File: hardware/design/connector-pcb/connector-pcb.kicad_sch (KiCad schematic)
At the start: 7 parts, among them J1 JWPF B04B, J2 JWPF B03B/B02B, J3 Conn_01x03_Pin, J5 Conn_01x02_Pin, J6 Conn_01x02_Pin, J8 JWPF B03B/B02B, J9 Conn_01x03_Pin

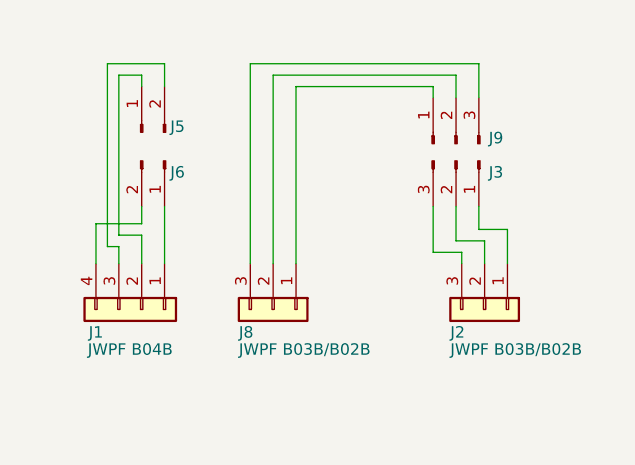
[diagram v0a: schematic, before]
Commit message: Gen2.1 final hardware design (#16)
* New schematic done

Works with TLIN1028-Q1 transceiver
Added BMP581 pressure sensor
Removed 3wire output stage

* FInal ordered hardware

New 3pin connector
Extra 2pin connector for cadence measurement
No 3pin sensor variant
DC/DC converter for MCU
Pressure sensor
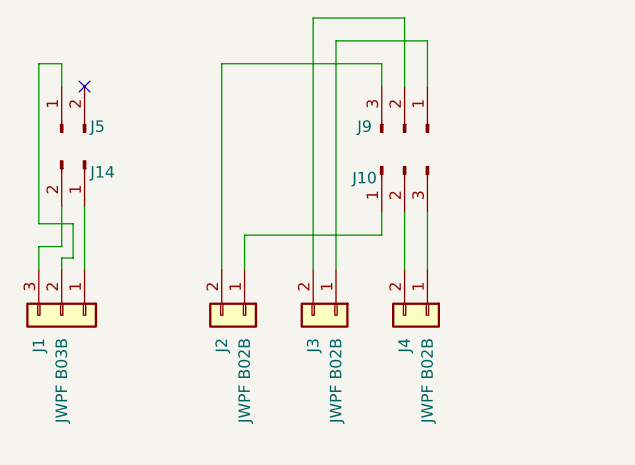
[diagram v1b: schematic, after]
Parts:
- removed J1: JWPF B04B, Connector_JST:JST_JWPF_B04B-JWPF-SK-R_1x04_P2.00mm_Vertical, symbol Connector_Generic:Conn_01x04
- removed J2: JWPF B03B/B02B, Connector_JST:JST_JWPF_B03B-JWPF-SK-R_1x03_P2.00mm_Vertical, symbol Connector_Generic:Conn_01x03
- added J1: JWPF B03B, Connector_JST:JST_JWPF_B03B-JWPF-SK-R_1x03_P2.00mm_Vertical, symbol Connector_Generic:Conn_01x03
- added J2, J3: JWPF B02B, Connector_JST:JST_JWPF_B02B-JWPF-SK-R_1x02_P2.00mm_Vertical, symbol Connector_Generic:Conn_01x02
- J4: renamed from J8; value JWPF B03B/B02B -> JWPF B02B; footprint Connector_JST:JST_JWPF_B03B-JWPF-SK-R_1x03_P2.00mm_Vertical -> Connector_JST:JST_JWPF_B02B-JWPF-SK-R_1x02_P2.00mm_Vertical; symbol Connector_Generic:Conn_01x03 -> Connector_Generic:Conn_01x02
- renumbered J3 to J10, J6 to J14
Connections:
- net at J10.1 (Pin_1): now also J2.1 (Pin_1)
- net at J10.2 (Pin_2): now also J4.2 (Pin_2)
- net at J10.3 (Pin_3): now also J4.1 (Pin_1)
- net at J5.1 (Pin_1): now also J1.2 (Pin_2)
- net at J9.1 (Pin_1): now also J3.1 (Pin_1); no longer J4.1 (Pin_1)
- net at J9.2 (Pin_2): now also J3.2 (Pin_2); no longer J4.2 (Pin_2)
- net at J9.3 (Pin_3): now also J2.2 (Pin_2); no longer J4.3 (Pin_3)
- net at J14.1 (Pin_1): now also J1.1 (Pin_1)
- net at J14.2 (Pin_2): now also J1.3 (Pin_3)
- no-connect marks 0 -> 1
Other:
- moved on the sheet: J10, J14, J5, J9
